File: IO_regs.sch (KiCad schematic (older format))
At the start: 77 parts, among them U227 74HC04, U228 74HC04, U229 74HC04, U230 74HC04, U231 74HC245, U232 74HC04, U233 74HC04, U234 74LS373, U43 74HC04, U44 74HC04, U47 74HC04, U50 74HC04, U51 74HC04, U52 74HC04

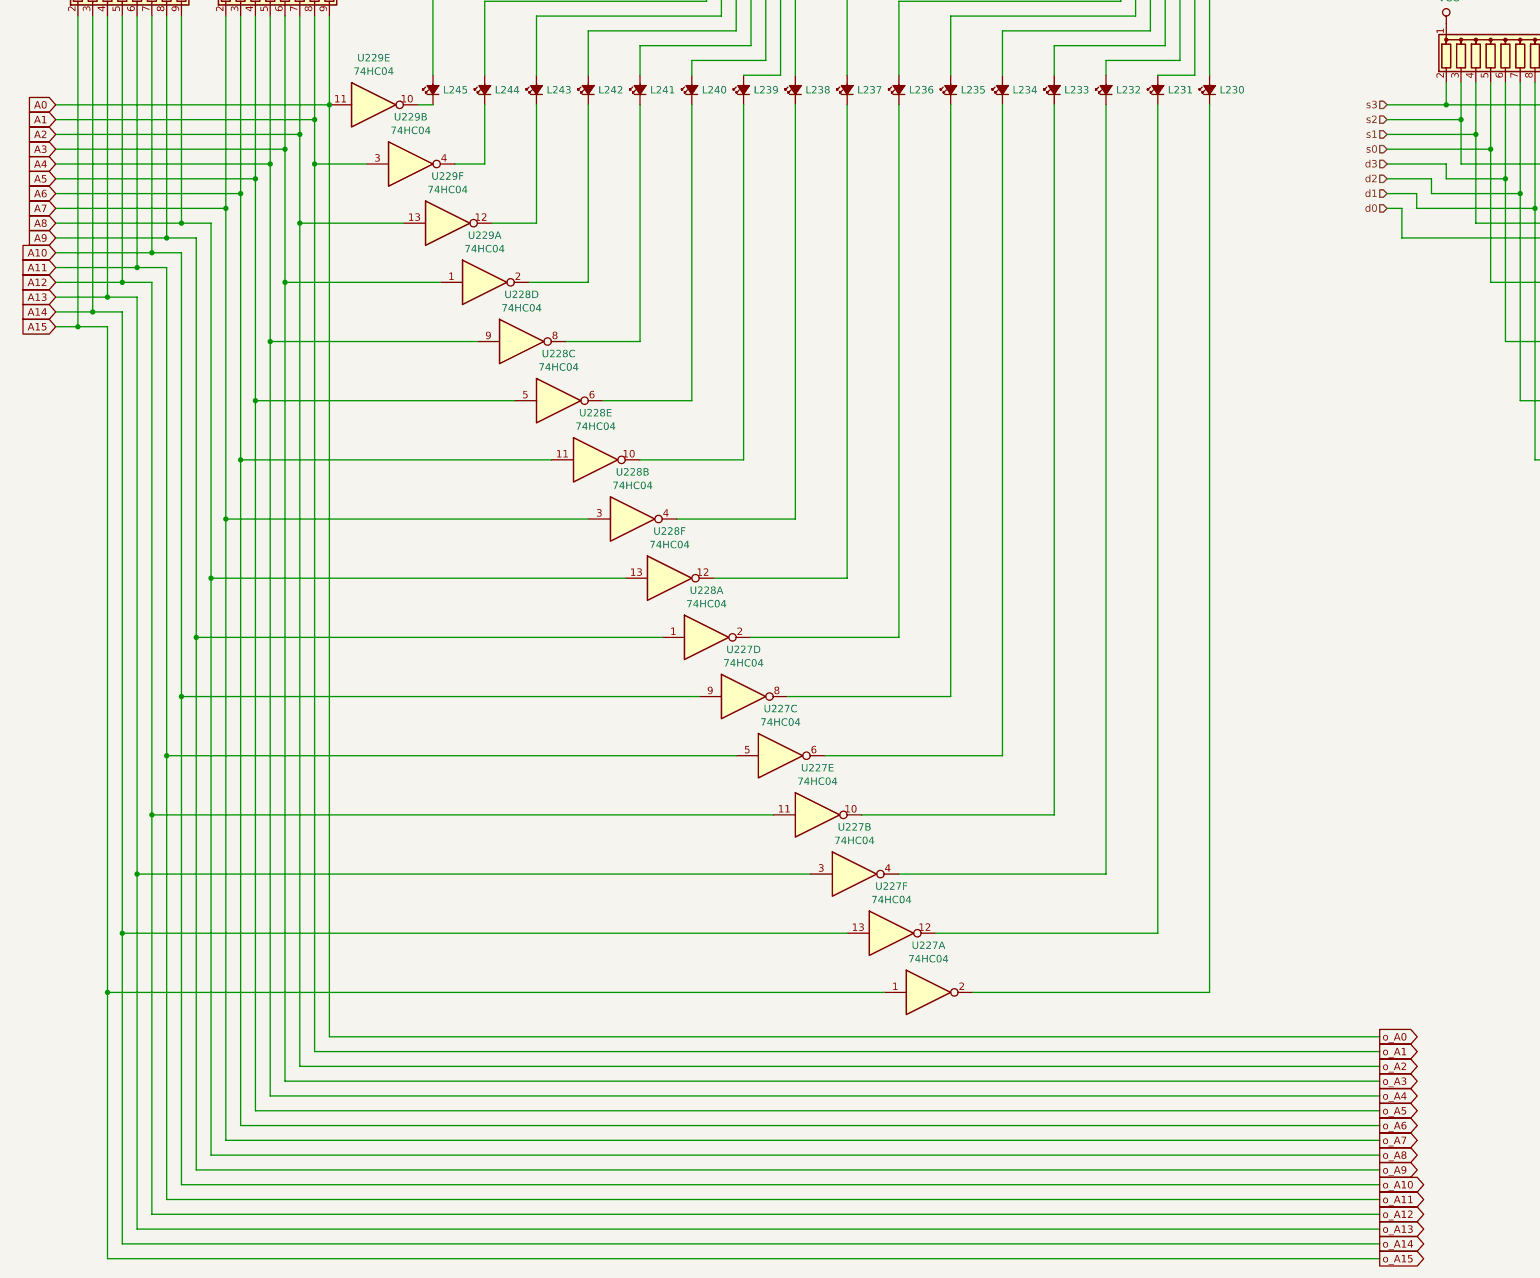
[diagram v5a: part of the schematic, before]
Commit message: oops, had to redo part of the PC because I inverted U182 and U195, also routed A0-A7 through the PC register
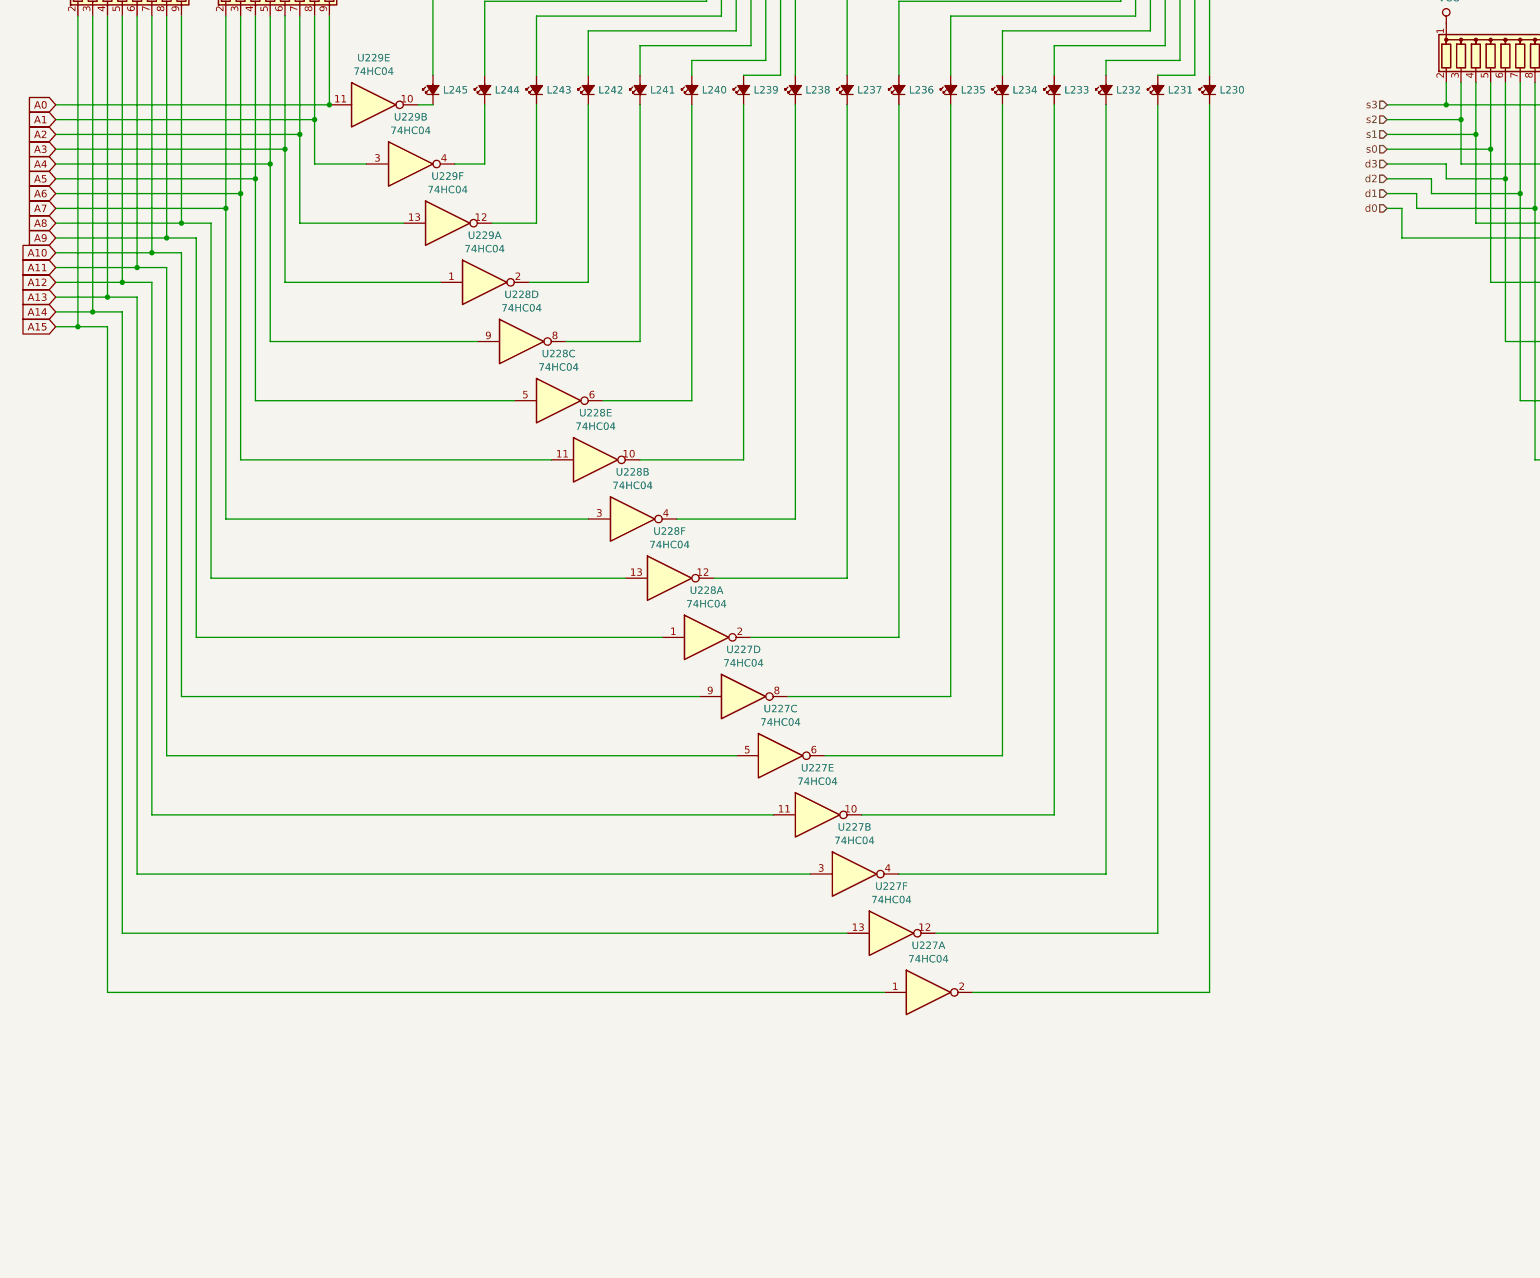
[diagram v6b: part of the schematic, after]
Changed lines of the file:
@@
-$EndComp
-$Comp
-L 74xx:74HC04 U227
-U 1 1 5E7F93C9
-P 6950 17200
-F 0 "U227" H 6950 17517 50  0000 C CNN
-F 1 "74HC04" H 6950 17426 50  0000 C CNN
-F 2 "Package_DIP:DIP-14_W7.62mm" H 6950 17200 50  0001 C CNN
-F 3 "https://assets.nexperia.com/documents/data-sheet/74HC_HCT04.pdf" H 6950 17200 50  0001 C CNN
-	1    6950 17200
-	1    0    0    -1
 $EndComp
 $Comp
@@
 Wire Wire Line
 	1400 17200 6650 17200
-Wire Wire Line
-	2900 11200 2900 17500
-Wire Wire Line
-	2900 17500 10000 17500
 Connection ~ 2900 11200
-Wire Wire Line
-	2800 11600 2800 17600
-Connection ~ 2800 11600
-Wire Wire Line
-	2700 12000 2700 17700
-Connection ~ 2700 12000
-Wire Wire Line
-	10000 17600 2800 17600
-Wire Wire Line
-	2700 17700 10000 17700
-Wire Wire Line
-	2600 12400 2600 17800
-Wire Wire Line
-	2600 17800 10000 17800
-Connection ~ 2600 12400
-Wire Wire Line
-	2500 12800 2500 17900
-Wire Wire Line
-	2500 17900 10000 17900
-Connection ~ 2500 12800
-Wire Wire Line
-	2400 13200 2400 18000
-Wire Wire Line
-	2400 18000 10000 18000
-Connection ~ 2400 13200
-Wire Wire Line
-	2300 13600 2300 18100
-Wire Wire Line
-	2300 18100 10000 18100
-Connection ~ 2300 13600
-Wire Wire Line
-	2200 14000 2200 18200
-Wire Wire Line
-	2200 18200 10000 18200
-Connection ~ 2200 14000
-Wire Wire Line
-	2100 14400 2100 18300
-Wire Wire Line
-	2100 18300 10000 18300
-Connection ~ 2100 14400
-Wire Wire Line
-	2000 14800 2000 18400
-Wire Wire Line
-	2000 18400 10000 18400
-Connection ~ 2000 14800
-Wire Wire Line
-	1900 15200 1900 18500
-Wire Wire Line
-	1900 18500 10000 18500
-Connection ~ 1900 15200
-Wire Wire Line
-	1800 15600 1800 18600
-Wire Wire Line
-	1800 18600 10000 18600
-Connection ~ 1800 15600
-Wire Wire Line
-	1700 16000 1700 18700
-Wire Wire Line
-	1700 18700 10000 18700
-Connection ~ 1700 16000
-Wire Wire Line
-	1600 16400 1600 18800
-Wire Wire Line
-	1600 18800 10000 18800
-Connection ~ 1600 16400
-Wire Wire Line
-	1500 16800 1500 18900
-Wire Wire Line
-	1500 18900 10000 18900
-Connection ~ 1500 16800
-Wire Wire Line
-	1400 17200 1400 19000
-Wire Wire Line
-	1400 19000 10000 19000
-Connection ~ 1400 17200
 $Comp
 L 74xx:74HC04 U230
@@
 Wire Wire Line
 	12050 1950 12050 3000
-Text GLabel 10000 17500 2    50   Output ~ 0
-o_A0
-Text GLabel 10000 17600 2    50   Output ~ 0
-o_A1
-Text GLabel 10000 17700 2    50   Output ~ 0
-o_A2
-Text GLabel 10000 17800 2    50   Output ~ 0
-o_A3
-Text GLabel 10000 17900 2    50   Output ~ 0
-o_A4
-Text GLabel 10000 18000 2    50   Output ~ 0
-o_A5
-Text GLabel 10000 18100 2    50   Output ~ 0
-o_A6
-Text GLabel 10000 18200 2    50   Output ~ 0
-o_A7
-Text GLabel 10000 18300 2    50   Output ~ 0
-o_A8
-Text GLabel 10000 18400 2    50   Output ~ 0
-o_A9
-Text GLabel 10000 18500 2    50   Output ~ 0
-o_A10
-Text GLabel 10000 18600 2    50   Output ~ 0
-o_A11
-Text GLabel 10000 18700 2    50   Output ~ 0
-o_A12
-Text GLabel 10000 18800 2    50   Output ~ 0
-o_A13
-Text GLabel 10000 18900 2    50   Output ~ 0
-o_A14
-Text GLabel 10000 19000 2    50   Output ~ 0
-o_A15
+$Comp
+L 74xx:74HC04 U227
+U 1 1 5E7F93C9
+P 6950 17200
+F 0 "U227" H 6950 17517 50  0000 C CNN
+F 1 "74HC04" H 6950 17426 50  0000 C CNN
+F 2 "Package_DIP:DIP-14_W7.62mm" H 6950 17200 50  0001 C CNN
+F 3 "https://assets.nexperia.com/documents/data-sheet/74HC_HCT04.pdf" H 6950 17200 50  0001 C CNN
+	1    6950 17200
+	1    0    0    -1
+$EndComp
 $EndSCHEMATC
